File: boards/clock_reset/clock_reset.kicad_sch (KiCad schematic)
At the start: 33 parts, among them J1 USB-MicroB-power, J2 signal_out, J3 uart_conn, J4 ICSP, SW1 green, SW2 yellow, SW3 red, SW4 white, SW5 white, U1 ATmega328P-P, U2 AQM0802A, Y1 16MHz

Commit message: assign footprints for clock_reset, and put board designs to one directory again
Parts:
- C1, C2, C3, C4, C5, C6, C7, C8: footprint (none) -> Capacitor_SMD:C_0805_2012Metric_Pad1.18x1.45mm_HandSolder
- D1: footprint (none) -> LED_SMD:LED_0805_2012Metric_Pad1.15x1.40mm_HandSolder
- D2: footprint (none) -> Diode_SMD:D_SOD-123
- J1: footprint (none) -> PrjLibrary:USB-MicroB-power
- J2, J3: footprint (none) -> Connector_PinHeader_2.54mm:PinHeader_1x06_P2.54mm_Vertical
- J4: footprint (none) -> Connector_PinHeader_2.54mm:PinHeader_2x03_P2.54mm_Vertical
- JP1: footprint (none) -> Connector_PinHeader_2.54mm:PinHeader_1x02_P2.54mm_Vertical
- R1, R10, R2, R3, R4, R5, R6, R7, R8, R9: footprint (none) -> Resistor_SMD:R_0805_2012Metric_Pad1.20x1.40mm_HandSolder
- SW1, SW2, SW3, SW4, SW5: footprint (none) -> Button_Switch_THT:SW_PUSH_6mm_H7.3mm
- U1: footprint Package_DIP:DIP-28_W7.62mm -> PrjLibrary:DIP-28_W7.62mm-D1mm
- U2: footprint (none) -> PrjLibrary:AQM0802A-RN-GBW
- Y1: footprint (none) -> Crystal:Crystal_HC49-4H_Vertical

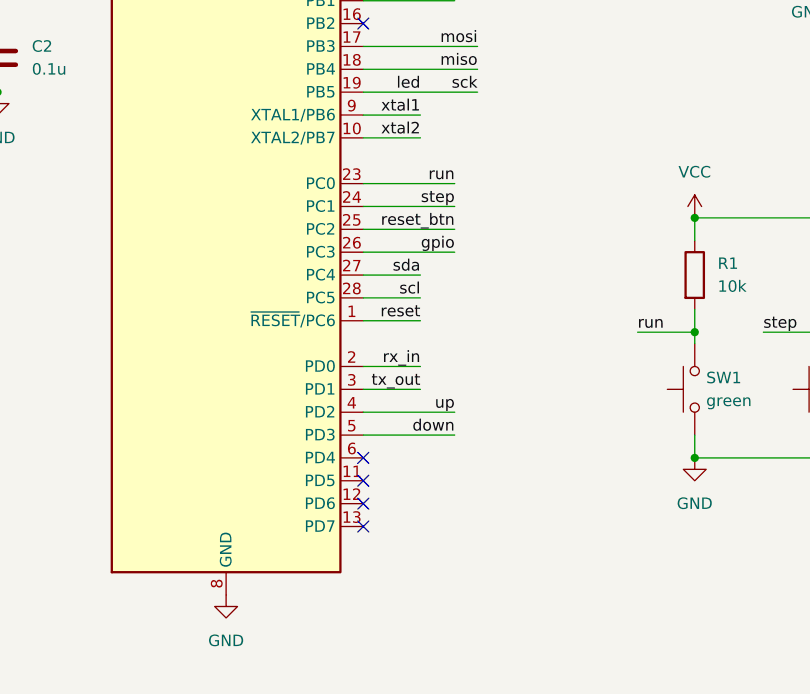
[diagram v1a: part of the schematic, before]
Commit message: clock_reset: add board design
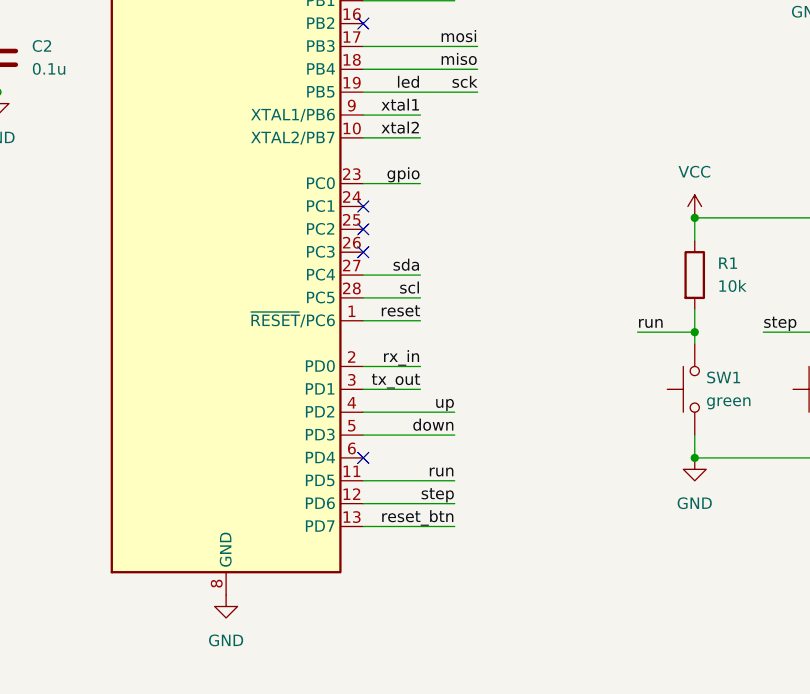
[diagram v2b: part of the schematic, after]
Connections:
- net gpio: now also U1.23 (PC0); no longer U1.26 (PC3)
- net reset_btn: now also U1.13 (PD7); no longer U1.25 (PC2)
- net run: now also U1.11 (PD5); no longer U1.23 (PC0)
- net step: now also U1.12 (PD6); no longer U1.24 (PC1)
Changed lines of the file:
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@@
   )
   (no_connect (at 158.75 137.16))
-  (no_connect (at 158.75 139.7))
-  (no_connect (at 158.75 142.24))
-  (no_connect (at 158.75 144.78))
   (no_connect (at 158.75 88.9))
   (no_connect (at 217.17 30.48))
+  (no_connect (at 158.75 109.22))
+  (no_connect (at 158.75 111.76))
+  (no_connect (at 158.75 114.3))
   (wire (pts (xy 158.75 96.52) (xy 171.45 96.52))
     (stroke (width 0) (type default) (color 0 0 0 0))
@@
     (stroke (width 0) (type default) (color 0 0 0 0))
   )
-  (wire (pts (xy 158.75 109.22) (xy 168.91 109.22))
+  (wire (pts (xy 158.75 142.24) (xy 168.91 142.24))
     (stroke (width 0) (type default) (color 0 0 0 0))
   )
@@
     (stroke (width 0) (type default) (color 0 0 0 0))
   )
-  (wire (pts (xy 158.75 111.76) (xy 168.91 111.76))
+  (wire (pts (xy 158.75 144.78) (xy 168.91 144.78))
     (stroke (width 0) (type default) (color 0 0 0 0))
   )
@@
     (stroke (width 0) (type default) (color 0 0 0 0))
   )
-  (wire (pts (xy 158.75 114.3) (xy 168.91 114.3))
+  (wire (pts (xy 158.75 106.68) (xy 165.1 106.68))
     (stroke (width 0) (type default) (color 0 0 0 0))
   )
@@
     (stroke (width 0) (type default) (color 0 0 0 0))
   )
-  (wire (pts (xy 158.75 106.68) (xy 168.91 106.68))
+  (wire (pts (xy 158.75 139.7) (xy 168.91 139.7))
     (stroke (width 0) (type default) (color 0 0 0 0))
   )
@@
     (effects (font (size 1.27 1.27)) (justify right bottom))
   )
-  (label "run" (at 168.91 106.68 180)
+  (label "run" (at 168.91 139.7 180)
     (effects (font (size 1.27 1.27)) (justify right bottom))
   )
@@
     (effects (font (size 1.27 1.27)) (justify right bottom))
   )
-  (label "step" (at 168.91 109.22 180)
+  (label "step" (at 168.91 142.24 180)
     (effects (font (size 1.27 1.27)) (justify right bottom))
   )
@@
     (effects (font (size 1.27 1.27)) (justify right bottom))
   )
-  (label "reset_btn" (at 168.91 111.76 180)
+  (label "reset_btn" (at 168.91 144.78 180)
     (effects (font (size 1.27 1.27)) (justify right bottom))
   )
@@
     (effects (font (size 1.27 1.27)) (justify right bottom))
   )
-  (label "gpio" (at 168.91 114.3 180)
-    (effects (font (size 1.27 1.27)) (justify right bottom))
-  )
+  (label "gpio" (at 165.1 106.68 180)
+    (effects (font (size 1.27 1.27)) (justify right bottom))
+  )

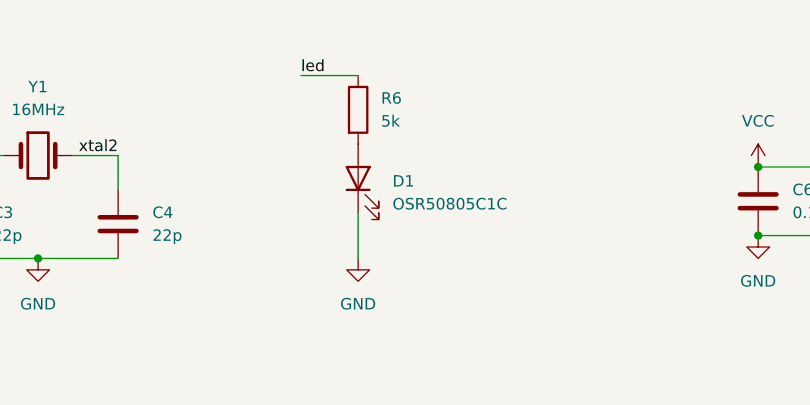
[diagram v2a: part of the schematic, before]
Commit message: change values according to actual parts
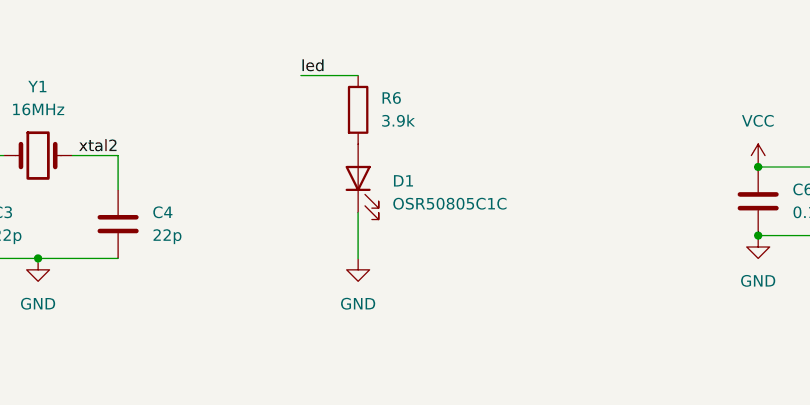
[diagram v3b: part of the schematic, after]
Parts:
- R6: value 5k -> 3.9k
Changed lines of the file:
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@@
       (effects (font (size 1.27 1.27)) (justify left))
     )
-    (property "Value" "5k" (id 1) (at 129.54 30.4799 0)
+    (property "Value" "3.9k" (id 1) (at 129.54 30.4799 0)
       (effects (font (size 1.27 1.27)) (justify left))
     )
@@
     )
     (path "/3bfbb178-5956-45ae-b486-c071c8b620fb"
-      (reference "R6") (unit 1) (value "5k") (footprint "Resistor_SMD:R_0805_2012Metric_Pad1.20x1.40mm_HandSolder")
+      (reference "R6") (unit 1) (value "3.9k") (footprint "Resistor_SMD:R_0805_2012Metric_Pad1.20x1.40mm_HandSolder")
     )
     (path "/bcc6f02b-1768-4467-8f74-0951fa710452"

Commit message: unify libraries
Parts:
- J1: footprint PrjLibrary:USB-MicroB-power -> MyLibrary:USB-MicroB-power
- U1: footprint PrjLibrary:DIP-28_W7.62mm-D1mm -> ModifiedKiCadLibrary:DIP-28_W7.62mm-D1mm
- U2: footprint PrjLibrary:AQM0802A-RN-GBW -> MyLibrary:AQM0802A-RN-GBW
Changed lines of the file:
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@@
       (effects (font (size 1.27 1.27)) (justify left))
     )
-    (property "Footprint" "PrjLibrary:AQM0802A-RN-GBW" (id 2) (at 224.79 40.64 0)
+    (property "Footprint" "MyLibrary:AQM0802A-RN-GBW" (id 2) (at 224.79 40.64 0)
       (effects (font (size 1.27 1.27)) hide)
     )
@@
     (property "Reference" "U1" (id 0) (at 121.92 77.47 0))
     (property "Value" "ATmega328P-P" (id 1) (at 121.92 80.01 0))
-    (property "Footprint" "PrjLibrary:DIP-28_W7.62mm-D1mm" (id 2) (at 143.51 114.3 0)
+    (property "Footprint" "ModifiedKiCadLibrary:DIP-28_W7.62mm-D1mm" (id 2) (at 143.51 114.3 0)
       (effects (font (size 1.27 1.27) italic) hide)
     )
@@
     (property "Reference" "J1" (id 0) (at 40.64 153.67 0))
     (property "Value" "USB-MicroB-power" (id 1) (at 40.64 156.21 0))
-    (property "Footprint" "PrjLibrary:USB-MicroB-power" (id 2) (at 40.64 163.83 0)
+    (property "Footprint" "MyLibrary:USB-MicroB-power" (id 2) (at 40.64 163.83 0)
       (effects (font (size 1.27 1.27)) hide)
     )
@@
     )
     (path "/d4f5f029-652f-436a-bb2c-81630291cef1"
-      (reference "J1") (unit 1) (value "USB-MicroB-power") (footprint "PrjLibrary:USB-MicroB-power")
+      (reference "J1") (unit 1) (value "USB-MicroB-power") (footprint "MyLibrary:USB-MicroB-power")
     )
     (path "/d46bba56-20eb-472a-859a-6f1cbbf3a02d"
@@
     )
     (path "/a90ad1b0-dd95-4cee-a717-3441df9bf56b"
-      (reference "U1") (unit 1) (value "ATmega328P-P") (footprint "PrjLibrary:DIP-28_W7.62mm-D1mm")
+      (reference "U1") (unit 1) (value "ATmega328P-P") (footprint "ModifiedKiCadLibrary:DIP-28_W7.62mm-D1mm")
     )
     (path "/0741ddd4-c1d6-44e7-9c69-2d2ac1c4abcb"
-      (reference "U2") (unit 1) (value "AQM0802A") (footprint "PrjLibrary:AQM0802A-RN-GBW")
+      (reference "U2") (unit 1) (value "AQM0802A") (footprint "MyLibrary:AQM0802A-RN-GBW")
     )
     (path "/ffe15c22-6549-4880-ae32-c2e96a1323c9"
